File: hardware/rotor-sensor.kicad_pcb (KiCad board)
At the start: 2 copper layers, 35.1 x 12.6 mm, 26 parts, among them J1 Conn_01x03, J2 Conn_01x03, J3 Conn_01x03, U1 ATtiny202-SS, U2 EE-SX1081, U3 SM351LT

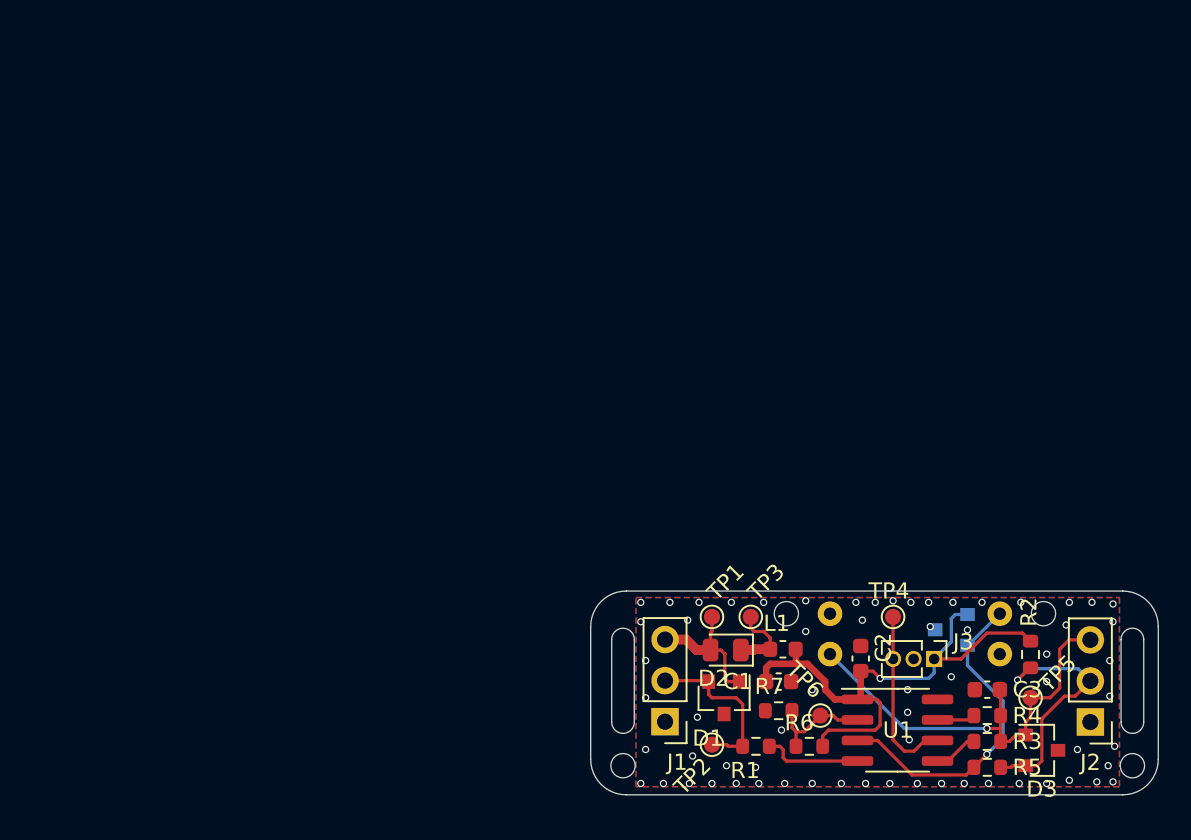
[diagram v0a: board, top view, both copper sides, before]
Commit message: Fixes DRC errors
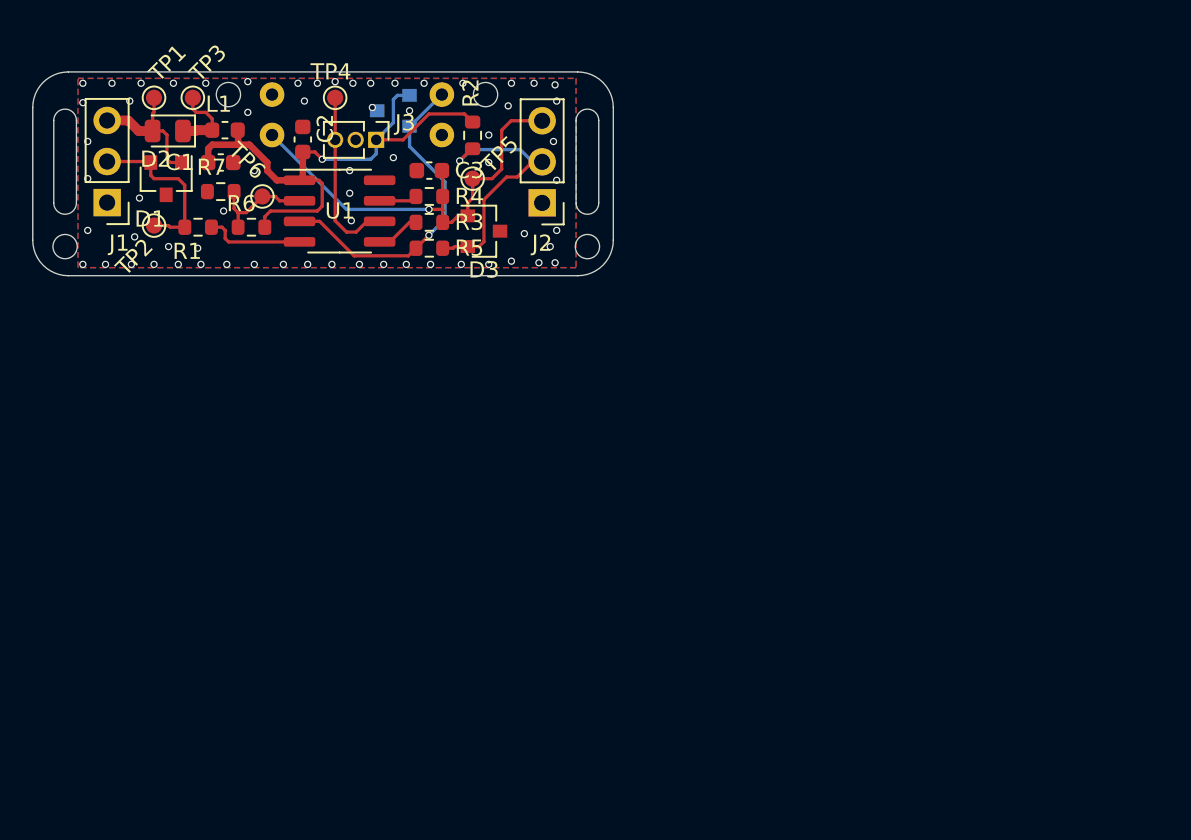
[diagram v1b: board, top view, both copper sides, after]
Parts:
- moved TP2 47.1 mm to (47.7, 33.8)
- moved C1 47.1 mm to (51.8, 29.9)
- moved C2 47.1 mm to (56.9, 28.5)
- moved C3 47.1 mm to (64.7, 30.4)
- moved D1 47.1 mm to (48.5, 30.9)
- moved D3 47.1 mm to (68.1, 34.1)
- moved J1 47.1 mm to (44.8, 32.4)
- moved J3 47.1 mm to (61.4, 28.5)
- moved L1 47.1 mm to (52.1, 27.9)
- moved R1 47.1 mm to (50.4, 33.9)
- moved R2 47.1 mm to (67.4, 28.2)
- moved R3 47.1 mm to (64.7, 33.6)
- moved TP1 47.1 mm to (47.7, 25.9)
- moved TP4 47.1 mm to (58.9, 25.9)
- moved TP5 47.1 mm to (67.4, 30.9)
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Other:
- board size 35.1 x 12.6 mm -> 35.9 x 12.6 mm

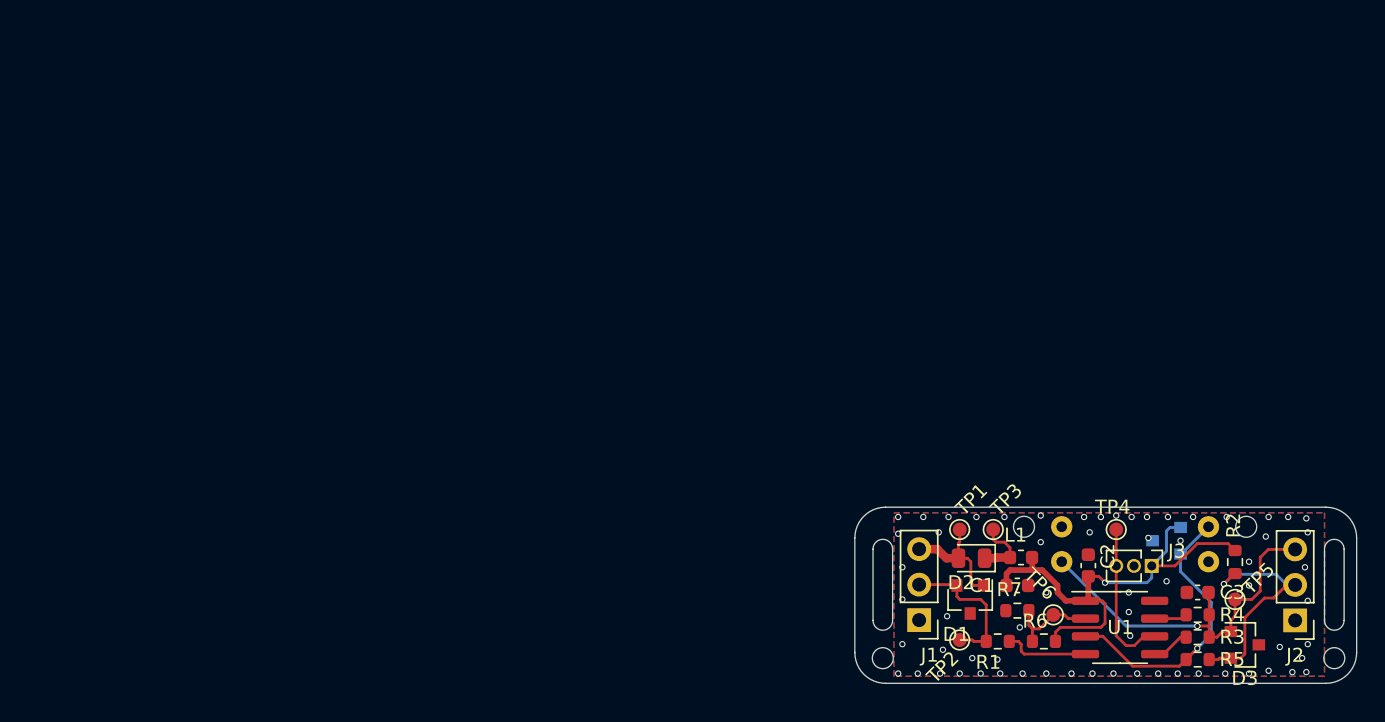
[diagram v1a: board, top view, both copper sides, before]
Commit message: Second hardware iteration
Cleaned up the schematic and reworked the entire PCB.
Replaced EE-SX1083 with EE-SX199, added 3D model and new component.
Added modified worksheet so that the PCB origin can be 0, 0.
Added scripts to execute certain tasks locally and updated the workflow accordingly.
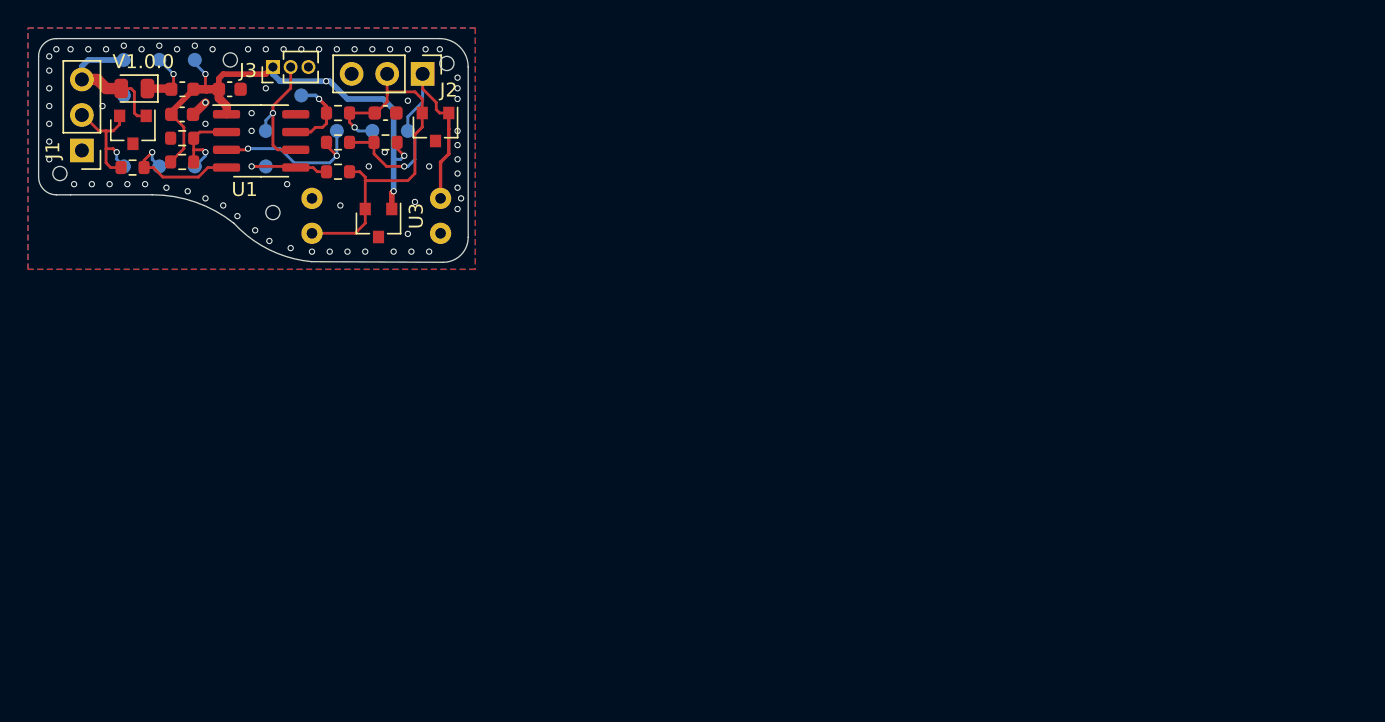
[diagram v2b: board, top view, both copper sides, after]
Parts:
- added TP10: AC-, TestPoint:TestPoint_Pad_D1.0mm, B.Cu at (-7.02, -0.08)
- added TP11: AC+, TestPoint:TestPoint_Pad_D1.0mm, B.Cu at (3.14, -2.62)
- added TP12: IN, TestPoint:TestPoint_Pad_D1.0mm, B.Cu at (8.22, -2.62)
- added TP13: OUT, TestPoint:TestPoint_Pad_D1.0mm, B.Cu at (5.68, -2.62)
- added TP7: COM, TestPoint:TestPoint_Pad_D1.0mm, B.Cu at (-9.56, -0.08)
- added TP8: W2, TestPoint:TestPoint_Pad_D1.0mm, B.Cu at (-1.94, -0.08)
- added TP9: SENSE, TestPoint:TestPoint_Pad_D1.0mm, B.Cu at (0.60, -5.16)
- TP1: value TestPoint_Alt -> +; moved to B.Cu
- TP2: value TestPoint_Alt -> COM; moved to B.Cu
- TP3: value TestPoint_Alt -> VD; moved to B.Cu
- TP4: value TestPoint_Alt -> VCC; moved to B.Cu
- TP5: value TestPoint_Alt -> -; moved to B.Cu
- TP6: value TestPoint_Alt -> UPDI; moved to B.Cu
- U2: value EE-SX1081 -> EE-SX199; footprint local:EE-SX1081 -> local:EE-SX199
- U3: moved to F.Cu
- moved TP5 87.3 mm to (-12.1, -5.16)
- moved TP4 74.0 mm to (-7.02, -7.70)
- moved J2 73.7 mm to (9.28, -6.70), turned to 270 degrees
- moved J3 72.3 mm to (-1.43, -7.19), turned to 90 degrees
- moved R5 71.8 mm to (3.23, -1.80)
- moved R4 71.2 mm to (3.23, -3.90)
- moved U1 70.6 mm to (-2.27, -1.91)
- moved R1 70.6 mm to (-11.5, 0.00)
- moved R6 70.5 mm to (-7.92, -0.40), turned to 0 degrees
- moved C2 70.2 mm to (-4.53, -5.60), turned to 0 degrees
- moved R3 69.9 mm to (3.23, 0.30)
- moved D3 68.7 mm to (10.2, -2.90), turned to 270 degrees
- moved TP2 68.7 mm to (-12.1, -0.08)
- moved L1 68.7 mm to (-7.91, -5.60)
- moved D1 68.7 mm to (-11.4, -2.70)
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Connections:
- net /Vin renamed Net-(D1-Pad1)
- C3 pad 1: Net-(C3-Pad1) -> /OS_OUTPUT
- D3 pad 1: Net-(C3-Pad1) -> /OS_INPUT
- D3 pad 2: Net-(D3-Pad2) -> /OS_OUTPUT
- J2 pad 1: GND -> /OS_INPUT
- J2 pad 2: Net-(D3-Pad2) -> /OS_OUTPUT
- J2 pad 3: Net-(C3-Pad1) -> GND
- J3 pad 2: GND -> PA0_UPDI
- J3 pad 3: Net-(J3-Pad3) -> GND
- R2 pad 1: Net-(D3-Pad2) -> /OS_INPUT
- R3 pad 2: Net-(C3-Pad1) -> /OS_OUTPUT
- R4 pad 2: Net-(C3-Pad1) -> /OS_OUTPUT
- R5 pad 2: Net-(D3-Pad2) -> /OS_INPUT
- TP4 pad 1: Net-(J3-Pad3) -> +5V
- TP5 pad 1: Net-(C3-Pad1) -> GND
- TP6 pad 1: PA6_AC0_AINN0 -> PA0_UPDI
- U1 pad 6: Net-(J3-Pad3) -> PA0_UPDI
- U2 pad 1: Net-(C3-Pad1) -> /OS_OUTPUT
- U2 pad 3: PA7_AC0_AINP0 -> /OS_INPUT
- U3 pad 2: PA7_AC0_AINP0 -> /OS_OUTPUT
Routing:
- net /OS_OUTPUT: track 0.00 -> 28.3 mm, vias 0 -> 1
- net Net-(C3-Pad1): track 26.4 -> 0.00 mm, vias 1 -> 0
- net /OS_INPUT: track 0.00 -> 23.2 mm, vias 0 -> 1
- net Net-(D3-Pad2): track 15.5 -> 0.00 mm, vias 1 -> 0
- net Net-(J3-Pad3): track 11.1 -> 0.00 mm
- net PA0_UPDI: track 0.00 -> 9.36 mm, vias 0 -> 1
- net PA7_AC0_AINP0: track 20.3 -> 11.6 mm, vias 1 -> 2
- net PA2_TCA2_W2: track 2.75 -> 6.53 mm, vias 0 -> 1
- net PA3_ADC0_AIN3: track 2.36 -> 5.80 mm, vias 0 -> 1
- net PA1_USART0_TXD: track 6.12 -> 9.03 mm, vias 0 -> 1
- net +5V: track 34.5 -> 37.3 mm, vias 1 -> 4
- net Net-(D1-Pad1): track 8.64 -> 10.8 mm
- net GND: track 0.00 -> 1.24 mm, vias 65 -> 73
- net Net-(D1-Pad2): track 10.4 -> 9.57 mm, vias 0 -> 1
- net Net-(D2-Pad1): track 4.68 -> 4.32 mm, vias 0 -> 1
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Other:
- board size 35.9 x 12.6 mm -> 30.7 x 16 mm
- board text added: "V1.0.0"

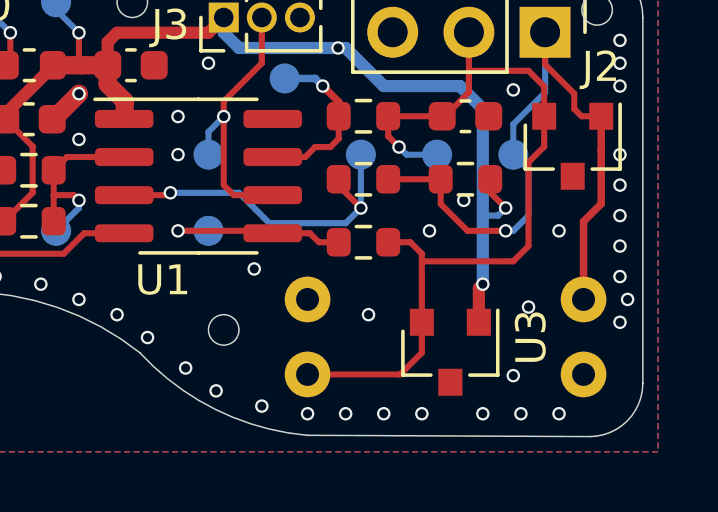
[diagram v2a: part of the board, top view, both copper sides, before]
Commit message: Increased clearance between Slot sensor and PCB edge
Assigned component values to remaining components.
Connectors will now only be placed in the DEBUG variant
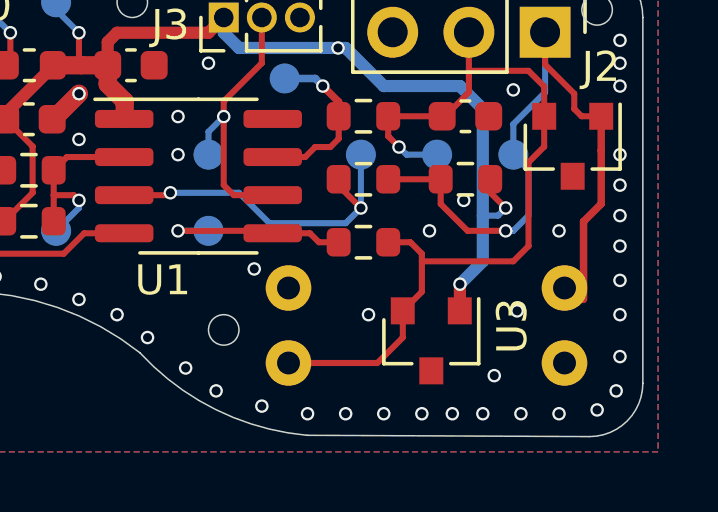
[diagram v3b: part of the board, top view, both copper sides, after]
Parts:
- moved U2 0.74 mm to (0.73, 4.33)
- moved U3 0.74 mm to (5.49, 3.59)
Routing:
- net GND: vias 73 -> 76
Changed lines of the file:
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@@
     (thickness 1.6)
     (drawings 17)
-    (tracks 251)
+    (tracks 255)
     (zones 0)
     (modules 33)
@@
     (32 B.Adhes user)
     (33 F.Adhes user)
-    (34 B.Paste user hide)
-    (35 F.Paste user hide)
+    (34 B.Paste user)
+    (35 F.Paste user)
     (36 B.SilkS user)
     (37 F.SilkS user)
@@
   )
   (setup
-    (last_trace_width 0.2032)
+    (last_trace_width 0.4064)
     (user_trace_width 0.2032)
     (user_trace_width 0.4064)
@@
   )
   (module local:EE-SX199 (layer B.Cu)
-    (at 1.362 4.706)
+    (at 0.727 4.325)
     (fp_text reference U2 (at 9.271 -4.659) (layer B.SilkS) hide
       (effects (font (size 1 1) (thickness 0.15)) (justify mirror))
@@
   )
   (module Package_TO_SOT_SMD:SOT-23 (layer F.Cu)
-    (at 6.122 3.968 270)
+    (at 5.487 3.587 270)
     (descr "SOT-23, Standard")
     (tags SOT-23)
@@
   (via (at 11.776 -0.588) (size 0.45) (drill 0.3) (layers F.Cu B.Cu) (net 1))
   (via (at 11.776 0.428) (size 0.45) (drill 0.3) (layers F.Cu B.Cu) (net 1))
-  (via (at 11.776 1.444) (size 0.45) (drill 0.3) (layers F.Cu B.Cu) (net 1))
-  (via (at 11.776 2.968) (size 0.45) (drill 0.3) (layers F.Cu B.Cu) (net 1))
-  (via (at 12.03 2.206) (size 0.45) (drill 0.3) (layers F.Cu B.Cu) (net 1))
+  (via (at 11.776 1.571) (size 0.45) (drill 0.3) (layers F.Cu B.Cu) (net 1))
+  (via (at 11.776 2.714) (size 0.45) (drill 0.3) (layers F.Cu B.Cu) (net 1))
   (via (at 5.172 6.016) (size 0.45) (drill 0.3) (layers F.Cu B.Cu) (net 1))
   (via (at 3.902 6.016) (size 0.45) (drill 0.3) (layers F.Cu B.Cu) (net 1))
@@
   (via (at -0.416 1.19) (size 0.45) (drill 0.3) (layers F.Cu B.Cu) (net 1))
   (via (at 3.394 2.714) (size 0.45) (drill 0.3) (layers F.Cu B.Cu) (net 1))
-  (via (at 8.22 4.746) (size 0.45) (drill 0.3) (layers F.Cu B.Cu) (net 1))
-  (via (at 8.728 2.46) (size 0.45) (drill 0.3) (layers F.Cu B.Cu) (net 1))
+  (via (at 7.585 4.746) (size 0.45) (drill 0.3) (layers F.Cu B.Cu) (net 1))
+  (via (at 8.347 2.587) (size 0.45) (drill 0.3) (layers F.Cu B.Cu) (net 1))
   (via (at 9.744 -0.08) (size 0.45) (drill 0.3) (layers F.Cu B.Cu) (net 1))
   (via (at 5.426 -0.08) (size 0.45) (drill 0.3) (layers F.Cu B.Cu) (net 1))
   (segment (start -7.11 -3.8) (end -6.258 -4.652) (width 0.6096) (layer F.Cu) (net 1))
   (segment (start -7.15 -3.8) (end -7.11 -3.8) (width 0.6096) (layer F.Cu) (net 1))
+  (via (at 11.776 4.111) (size 0.45) (drill 0.3) (layers F.Cu B.Cu) (net 1))
+  (via (at 11.649 5.254) (size 0.45) (drill 0.3) (layers F.Cu B.Cu) (net 1))
+  (via (at 11.014 5.889) (size 0.45) (drill 0.3) (layers F.Cu B.Cu) (net 1))
+  (via (at 6.188 6.016) (size 0.45) (drill 0.3) (layers F.Cu B.Cu) (net 1))
   (segment (start -7.125 -5.6) (end -7.125 -5.563) (width 0.4064) (layer F.Cu) (net 2))
   (segment (start -8.7 -3.988) (end -8.7 -3.8) (width 0.4064) (layer F.Cu) (net 2))
@@
   (segment (start 3.902 -4.906) (end 6.442 -4.906) (width 0.4064) (layer B.Cu) (net 2))
   (segment (start 6.442 -4.906) (end 7.204 -4.144) (width 0.4064) (layer B.Cu) (net 2))
-  (via (at 7.204 1.698) (size 0.45) (drill 0.3) (layers F.Cu B.Cu) (net 2))
-  (segment (start 7.072 1.83) (end 7.204 1.698) (width 0.4064) (layer F.Cu) (net 2))
-  (segment (start 7.072 2.968) (end 7.072 1.83) (width 0.4064) (layer F.Cu) (net 2))
   (via (at 7.966 -0.842) (size 0.45) (drill 0.3) (layers F.Cu B.Cu) (net 2))
   (segment (start 7.45 -1.358) (end 7.966 -0.842) (width 0.2032) (layer F.Cu) (net 2))
@@
   (segment (start 7.712 -0.588) (end 7.204 -0.588) (width 0.2032) (layer B.Cu) (net 2))
   (segment (start 7.966 -0.842) (end 7.712 -0.588) (width 0.2032) (layer B.Cu) (net 2))
-  (segment (start 7.204 -0.588) (end 7.204 1.698) (width 0.4064) (layer B.Cu) (net 2))
   (segment (start 7.204 -4.144) (end 7.204 -0.588) (width 0.4064) (layer B.Cu) (net 2))
   (segment (start 2.378 -6.176) (end 2.632 -6.176) (width 0.4064) (layer B.Cu) (net 2))
   (via (at 2.378 -6.176) (size 0.45) (drill 0.3) (layers F.Cu B.Cu) (net 2))
+  (segment (start 6.442 1.698) (end 6.437 2.587) (width 0.4064) (layer F.Cu) (net 2))
+  (via (at 6.442 1.698) (size 0.45) (drill 0.3) (layers F.Cu B.Cu) (net 2))
+  (segment (start 7.204 0.936) (end 7.204 -0.588) (width 0.4064) (layer B.Cu) (net 2))
+  (segment (start 6.442 1.698) (end 7.204 0.936) (width 0.4064) (layer B.Cu) (net 2))
   (segment (start -13.878 -2.62) (end -13.37 -2.62) (width 0.2032) (layer F.Cu) (net 3))
   (segment (start -15.018 -3.76) (end -13.878 -2.62) (width 0.2032) (layer F.Cu) (net 3))
@@
   (segment (start 4.05 0.3) (end 4.79 0.3) (width 0.2032) (layer F.Cu) (net 10))
   (segment (start 4.79 0.3) (end 5.172 0.682) (width 0.2032) (layer F.Cu) (net 10))
-  (segment (start 5.172 2.968) (end 5.172 3.984) (width 0.2032) (layer F.Cu) (net 10))
-  (segment (start 4.45 4.706) (end 1.362 4.706) (width 0.2032) (layer F.Cu) (net 10))
-  (segment (start 5.172 3.984) (end 4.45 4.706) (width 0.2032) (layer F.Cu) (net 10))
   (segment (start 9.25 -3.9) (end 9.25 -2.888) (width 0.2032) (layer F.Cu) (net 10))
   (segment (start 9.25 -2.888) (end 8.728 -2.366) (width 0.2032) (layer F.Cu) (net 10))
@@
   (segment (start 8.728 0.428) (end 8.22 0.936) (width 0.2032) (layer F.Cu) (net 10))
   (segment (start 8.22 0.936) (end 5.172 0.936) (width 0.2032) (layer F.Cu) (net 10))
-  (segment (start 5.172 0.936) (end 5.172 2.968) (width 0.2032) (layer F.Cu) (net 10))
   (segment (start 5.172 0.682) (end 5.172 0.936) (width 0.2032) (layer F.Cu) (net 10))
   (via (at 4.41 -2.874) (size 0.45) (drill 0.3) (layers F.Cu B.Cu) (net 10))
@@
   (segment (start 8.728 -5.414) (end 6.784 -5.414) (width 0.2032) (layer F.Cu) (net 10))
   (segment (start 9.25 -3.9) (end 9.25 -4.892) (width 0.2032) (layer F.Cu) (net 10))
+  (segment (start 5.172 1.952) (end 4.537 2.587) (width 0.2032) (layer F.Cu) (net 10))
+  (segment (start 5.172 0.936) (end 5.172 1.952) (width 0.2032) (layer F.Cu) (net 10))
+  (segment (start 4.537 2.587) (end 4.537 3.476) (width 0.2032) (layer F.Cu) (net 10))
+  (segment (start 3.688 4.325) (end 0.727 4.325) (width 0.2032) (layer F.Cu) (net 10))
+  (segment (start 4.537 3.476) (end 3.688 4.325) (width 0.2032) (layer F.Cu) (net 10))
   (segment (start 11.15 -3.9) (end 10.496 -3.9) (width 0.2032) (layer F.Cu) (net 11))
   (segment (start 10.496 -3.9) (end 10.252 -4.144) (width 0.2032) (layer F.Cu) (net 11))
